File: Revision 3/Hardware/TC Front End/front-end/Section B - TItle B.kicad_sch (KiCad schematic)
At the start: 0 parts

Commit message: Project template fully initialized
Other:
- note removed: "References:"

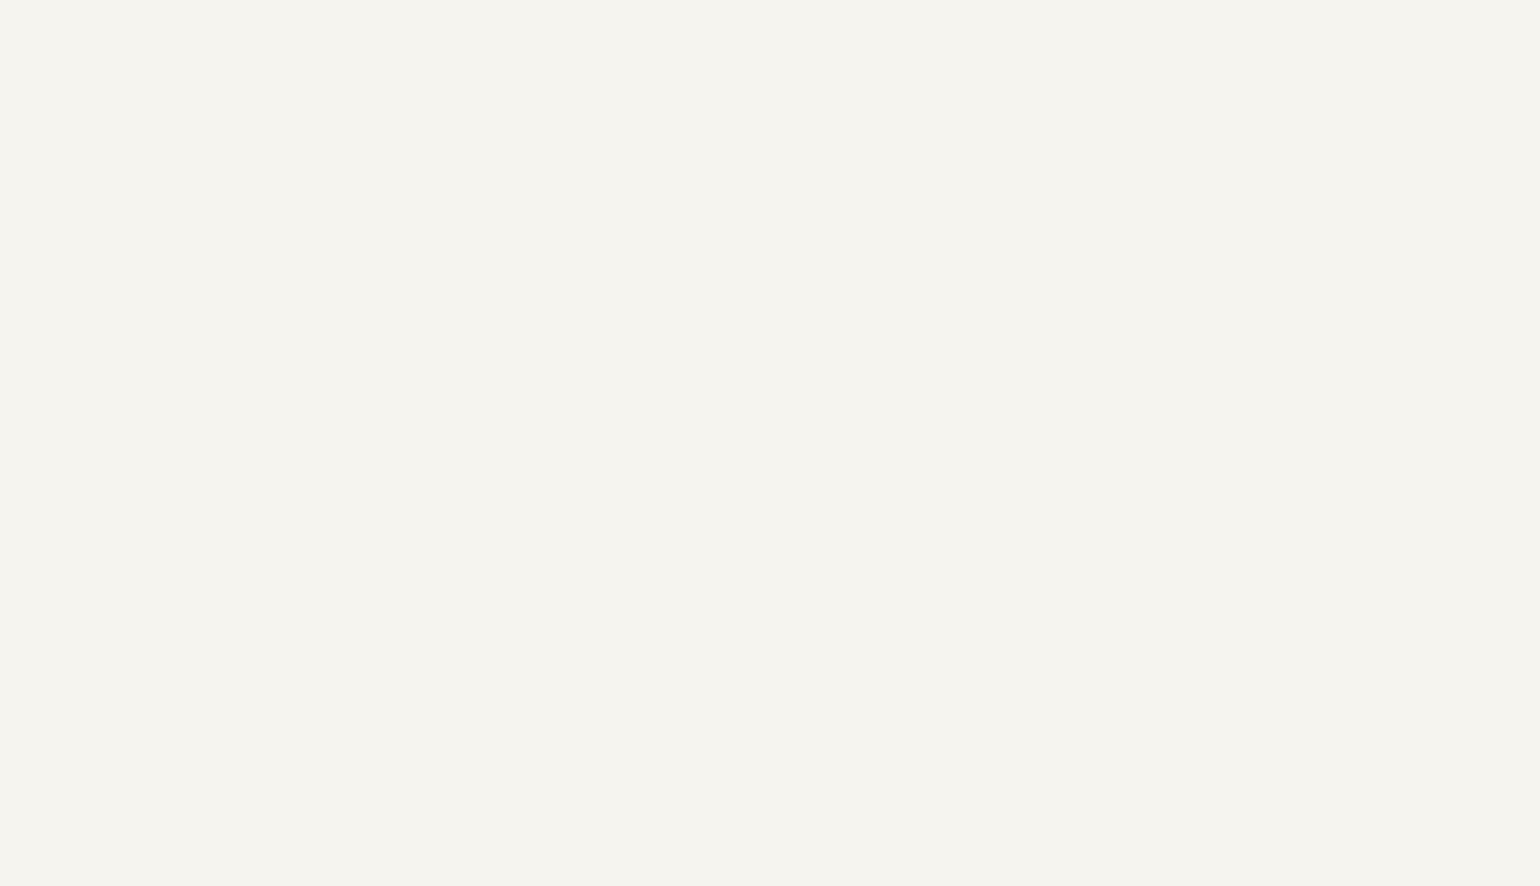
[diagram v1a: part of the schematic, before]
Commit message: Analog schematic substantially complete
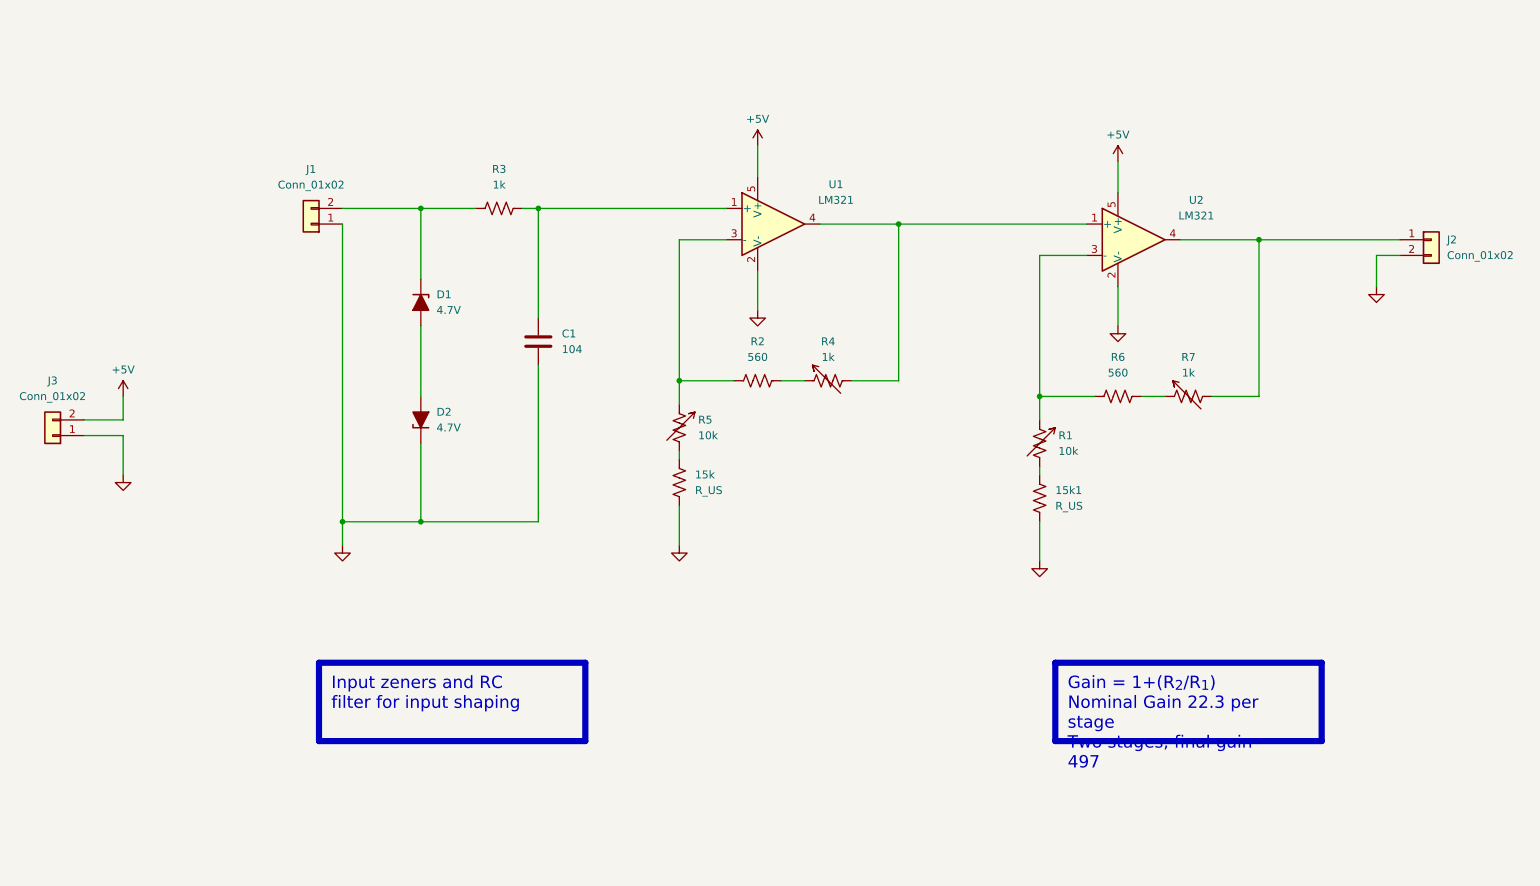
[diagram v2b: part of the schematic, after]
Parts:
- added 15k, 15k1: R_US, symbol Device:R_US
- added C1: 104, symbol Device:C
- added D1, D2: 4.7V, symbol Device:D_Zener_Filled
- added J1, J2, J3: Conn_01x02, symbol Connector_Generic:Conn_01x02
- added R1, R5: 10k, symbol Device:R_Variable_US
- added R2, R6: 560, symbol Device:R_US
- added R3: 1k, symbol Device:R_US
- added R4, R7: 1k, symbol Device:R_Variable_US
- added U1, U2: LM321, Package_TO_SOT_SMD:SOT-23-5, symbol Amplifier_Operational:LM321
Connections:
- new net: R1.1, R6.1, U2.3 (-)
- new net: R6.2, R7.1
- new net: D1.1 (K), J1.2 (Pin_2), R3.1
- new net: C1.1, R3.2, U1.1 (+)
- new net: 15k1.1, R1.2
- new net: J2.1 (Pin_1), R7.2, U2.4
- new net: R2.1, R5.1, U1.3 (-)
- new net: 15k.1, R5.2
- new net: R2.2, R4.1
- new net: R4.2, U1.4, U2.1 (+)
- new net: D1.2 (A), D2.2 (A)
- new net +5V: J3.2 (Pin_2), U1.5 (V+), U2.5 (V+)
- new net GND: 15k.2, 15k1.2, C1.2, D2.1 (K), J1.1 (Pin_1), J2.2 (Pin_2), J3.1 (Pin_1), U1.2 (V-), U2.2 (V-)
